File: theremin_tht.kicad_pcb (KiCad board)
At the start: 2 copper layers, 139.7 x 38.1 mm, 108 parts, among them J1 Audio Out, J2 12VAC, Q1 2N3904, Q2 2N3904, Q3 2N3904, Q4 2N3904, Q5 2N3904, Q6 2N3904, Q7 2N3904, Q8 2N3904, SW1 SW_SPDT, U1 LM13600, U2 L7812, U3 L7912

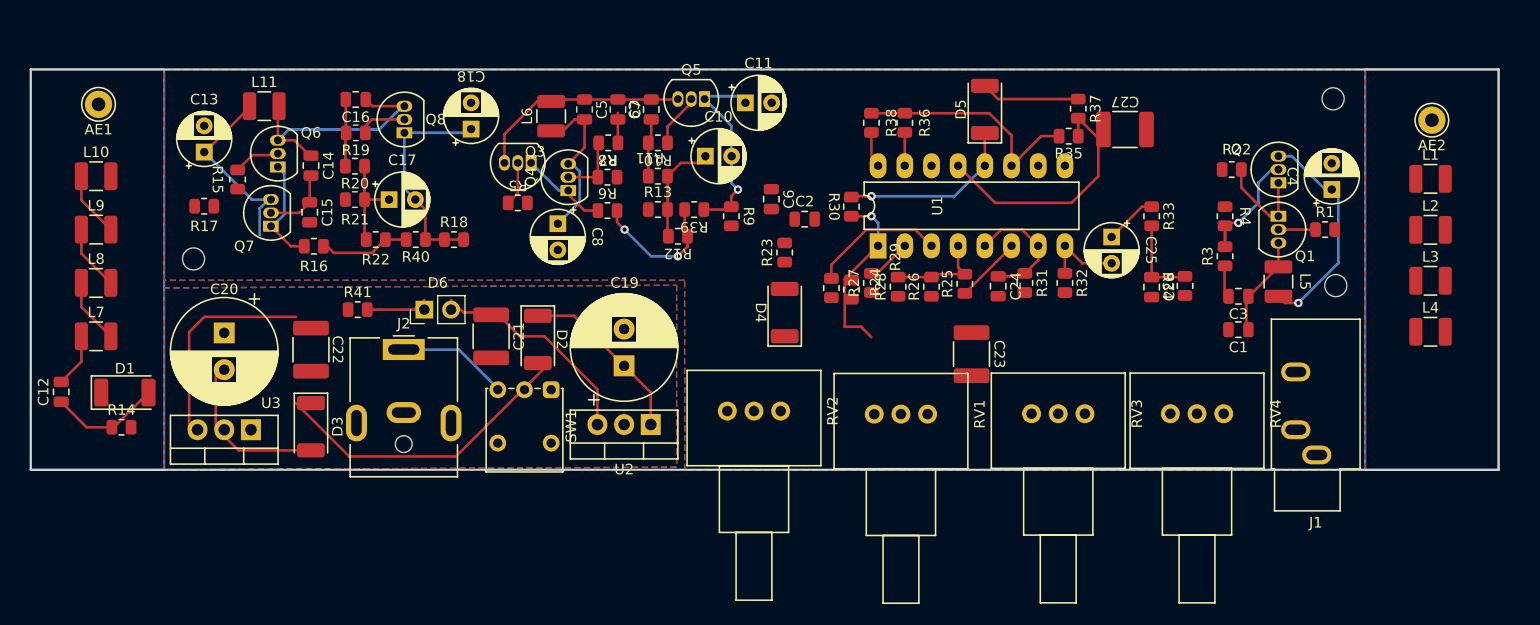
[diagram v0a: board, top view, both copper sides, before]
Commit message: Layout cleanup for smd and through
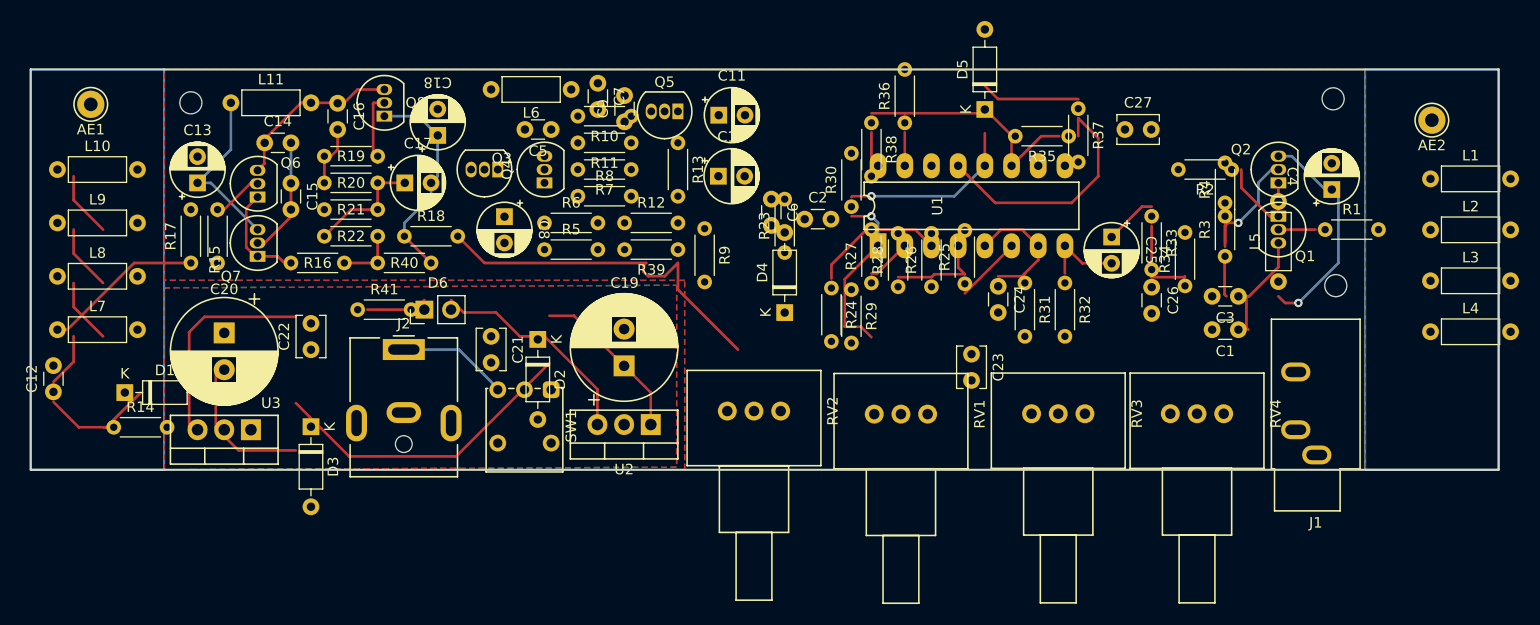
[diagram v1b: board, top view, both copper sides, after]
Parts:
- C1, C12, C14, C15, C16, C2, C24, C26, C3, C5, C6, C7, C9: footprint Capacitor_SMD:C_0805_2012Metric -> Capacitor_THT:C_Disc_D3.0mm_W1.6mm_P2.50mm
- C21, C22, C23, C27: footprint Capacitor_SMD:C_1812_4532Metric -> Capacitor_THT:C_Disc_D3.8mm_W2.6mm_P2.50mm
- D1, D2, D3, D4, D5: footprint Diode_SMD:D_2010_5025Metric -> Diode_THT:D_DO-35_SOD27_P7.62mm_Horizontal
- L1, L10, L11, L2, L3, L4, L5, L6, L7, L8, L9: footprint Inductor_SMD:L_1210_3225Metric -> Inductor_THT:L_Axial_L5.3mm_D2.2mm_P7.62mm_Horizontal_Vishay_IM-1
- R1, R10, R11, R12, R13, R14, R15, R16, R17, R18, R19, R2, R20, R21, R22, R23, R24, R25, R26, R27, R28, R29, R3, R30, R31, R32, R33, R34, R35, R36, R37, R38, R39, R4, R40, R41, R5, R6, R7, R8, R9: footprint Resistor_SMD:R_0805_2012Metric -> Resistor_THT:R_Axial_DIN0204_L3.6mm_D1.6mm_P5.08mm_Horizontal
- moved REF** 14.9 mm to (40.6, 28.6)
- moved R13 6.63 mm to (87.0, 32.4), turned to -90 degrees
- moved R6 6.11 mm to (74.3, 40.0)
- moved R17 5.54 mm to (40.6, 43.8), turned to 90 degrees
- moved R12 5.24 mm to (81.9, 40.0), turned to 0 degrees
- moved C8 5.12 mm to (70.5, 39.4)
- moved R5 5.12 mm to (74.3, 42.5)
- moved C14 4.91 mm to (47.7, 32.4), turned to 0 degrees
- moved R18 4.73 mm to (61.0, 41.3)
- moved R39 4.11 mm to (87.0, 42.5)
- moved R11 4.07 mm to (82.5, 32.4)
- moved L10 3.73 mm to (27.9, 34.9)
- moved L7 3.73 mm to (27.9, 50.2)
- moved L8 3.73 mm to (27.9, 45.1)
- moved L9 3.73 mm to (27.9, 40.0)
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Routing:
- net Volume Tuning: track 0.00 -> 34.5 mm
- net Volume Antenna B: track 5.13 -> 26.7 mm
- net Net-(Q3-C): track 20.9 -> 0.00 mm
- net Net-(Q5-E): track 19.1 -> 0.00 mm, vias 1 -> 0
- net +12V: track 98.9 -> 81.3 mm
- net -12V: track 47.7 -> 30.7 mm, vias 2 -> 0
- net Net-(C10-Pad1): track 8.61 -> 0.00 mm
- net Net-(Q3-E): track 8.44 -> 0.00 mm
- net Net-(Q6-C): track 23.9 -> 17.1 mm
- net Net-(L10-Pad1): track 6.24 -> 0.00 mm
- net Net-(Q4-B): track 6.19 -> 0.00 mm
- net Net-(C9-Pad1): track 5.51 -> 0.00 mm
- net Net-(Q5-B): track 5.11 -> 0.00 mm
- net Net-(Q3-B): track 4.19 -> 0.00 mm
- net Net-(Q7-B): track 7.31 -> 10.7 mm
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
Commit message: Small update
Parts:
- moved R13 5.10 mm to (89.5, 36.8), turned to 180 degrees
- moved C9 4.56 mm to (78.1, 27.9)
- moved Q5 3.05 mm to (87.6, 32.4)
- moved L6 2.05 mm to (74.9, 27.9)
- moved C7 1.77 mm to (80.6, 25.4)
- moved R24 1.55 mm to (101.6, 44.7)
- moved R30 1.55 mm to (103.5, 36.9)
- moved C2 1.55 mm to (99.1, 38.1)
- moved C23 1.55 mm to (114.9, 50.9)
- moved C24 1.55 mm to (117.5, 44.5)
- moved C25 1.55 mm to (128.3, 39.8)
- moved C26 1.55 mm to (132.1, 44.6)
- moved C27 1.55 mm to (129.5, 29.6)
- moved C6 1.55 mm to (95.9, 36.2)
- moved R23 1.55 mm to (97.2, 41.3)
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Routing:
- net Net-(Q3-C): track 0.00 -> 29.6 mm
- net +12V: track 81.3 -> 88.7 mm
- net Net-(C7-Pad2): track 0.00 -> 7.03 mm
- net Volume Tuning: track 34.5 -> 31.5 mm
- net Net-(C9-Pad1): track 0.00 -> 2.54 mm
